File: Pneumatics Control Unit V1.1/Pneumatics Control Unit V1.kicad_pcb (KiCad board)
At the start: 2 copper layers, 53.6 x 65.4 mm, 80 parts, among them J1 TX_PORT, J10 Conn_01x02_Male, J11 Conn_01x02_Male, J12 10118194-0001LF, J2 RX_PORT, J3 MICROMOD-2222, J4 Conn_01x02_Male, J5 Conn_01x02_Male, J6 Conn_01x02_Male, J7 Conn_01x02_Male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

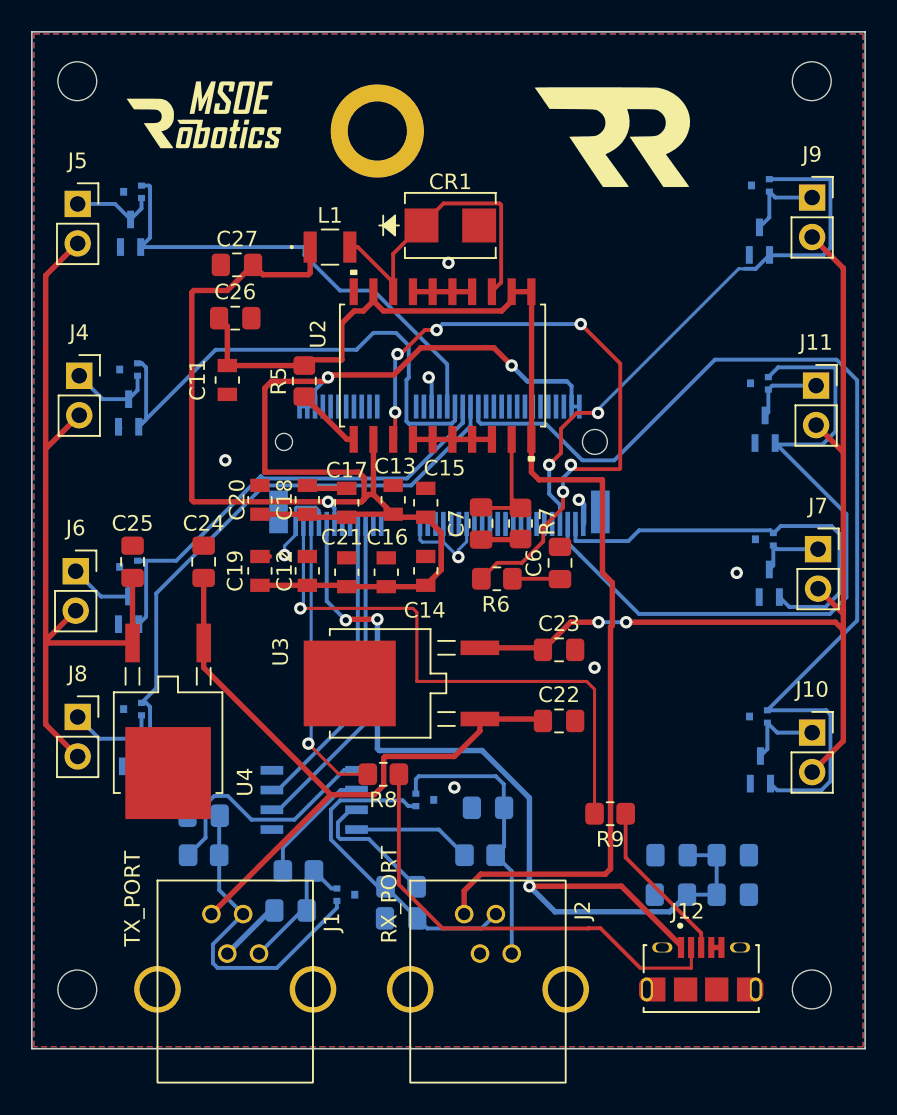
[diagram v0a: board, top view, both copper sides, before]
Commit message: Adding more grounding vias, and making the mouting holes 8-32
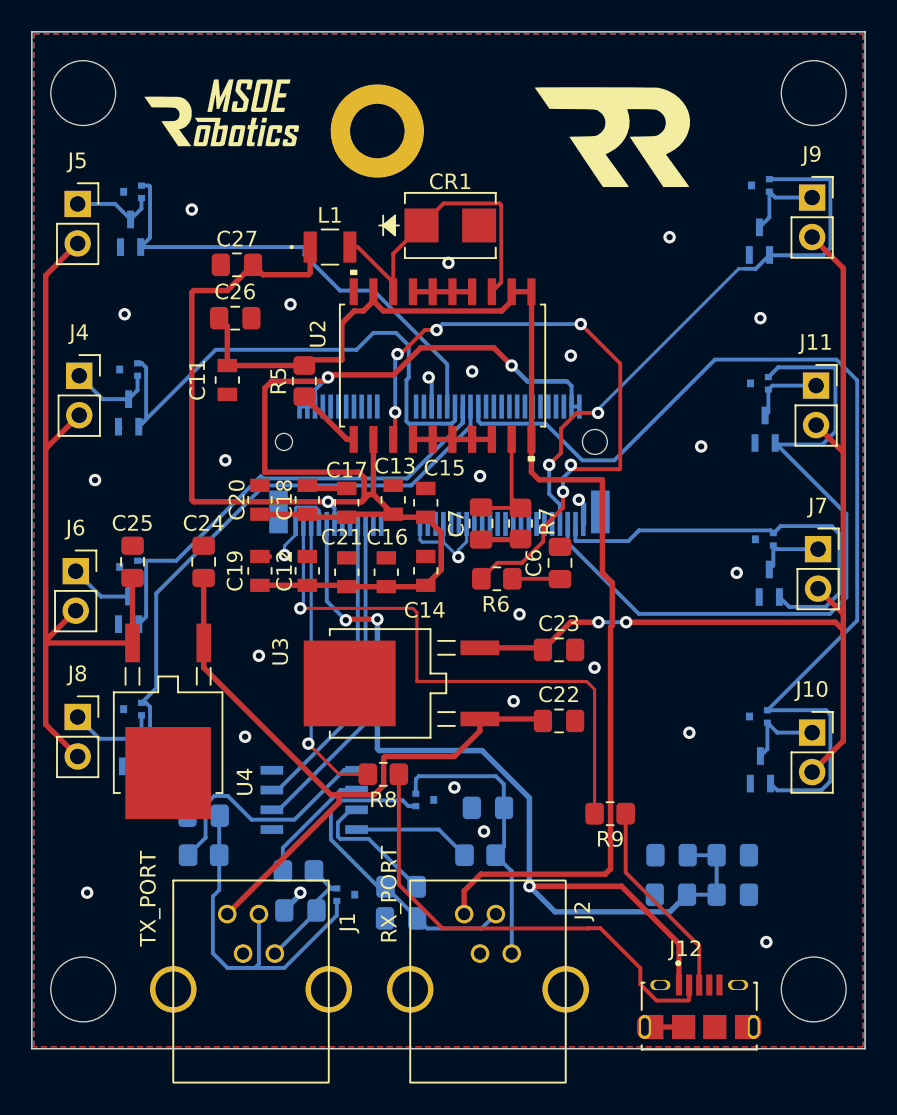
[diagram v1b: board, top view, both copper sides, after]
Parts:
- moved J12 2.42 mm to (146.7, 129.4)
- moved G*** 1.15 mm to (116.0, 70.6)
- moved J1 1.02 mm to (117.9, 128.7)
- moved H2 0.85 mm to (107.1, 69.3)
- moved H1 0.77 mm to (154.1, 69.3)
- moved C3 0.64 mm to (121.0, 121.9)
- moved H4 0.38 mm to (107.1, 127.0)
- moved H3 0.13 mm to (154.1, 127.0)
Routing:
- net USB_V: track 62.9 -> 65.2 mm
- net Net-(J12-Pad3): track 10.6 -> 13.0 mm
- net Net-(C1-Pad1): track 21.1 -> 23.3 mm
- net GND: track 38.1 -> 36.9 mm, vias 9 -> 28
- net Net-(J12-Pad2): track 29.5 -> 30.4 mm
- net Net-(C3-Pad1): track 8.89 -> 8.06 mm

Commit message: Adding Raider Robotics, removing Vex U
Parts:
- removed the G*** at (116.0, 70.6)
- removed the G*** at (143.0, 74.5)

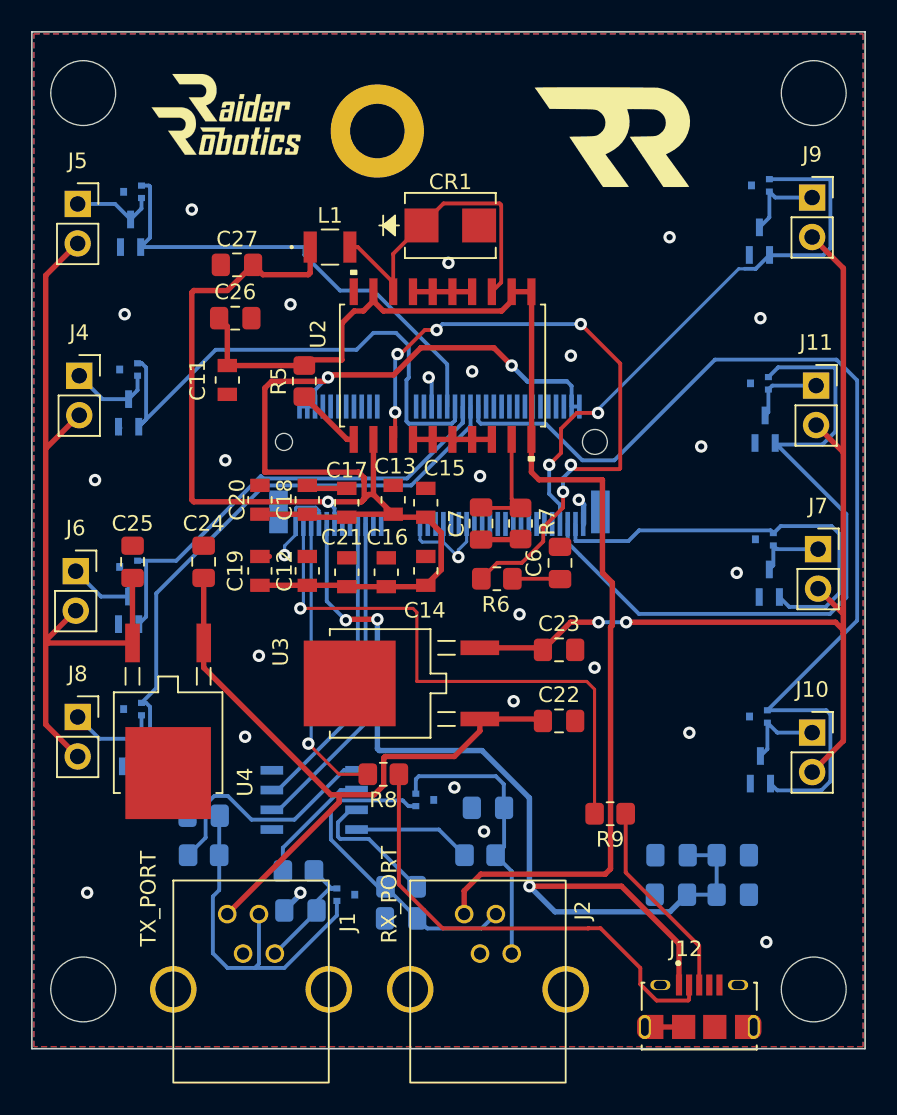
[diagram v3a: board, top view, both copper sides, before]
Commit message: Adding 12V capabilities
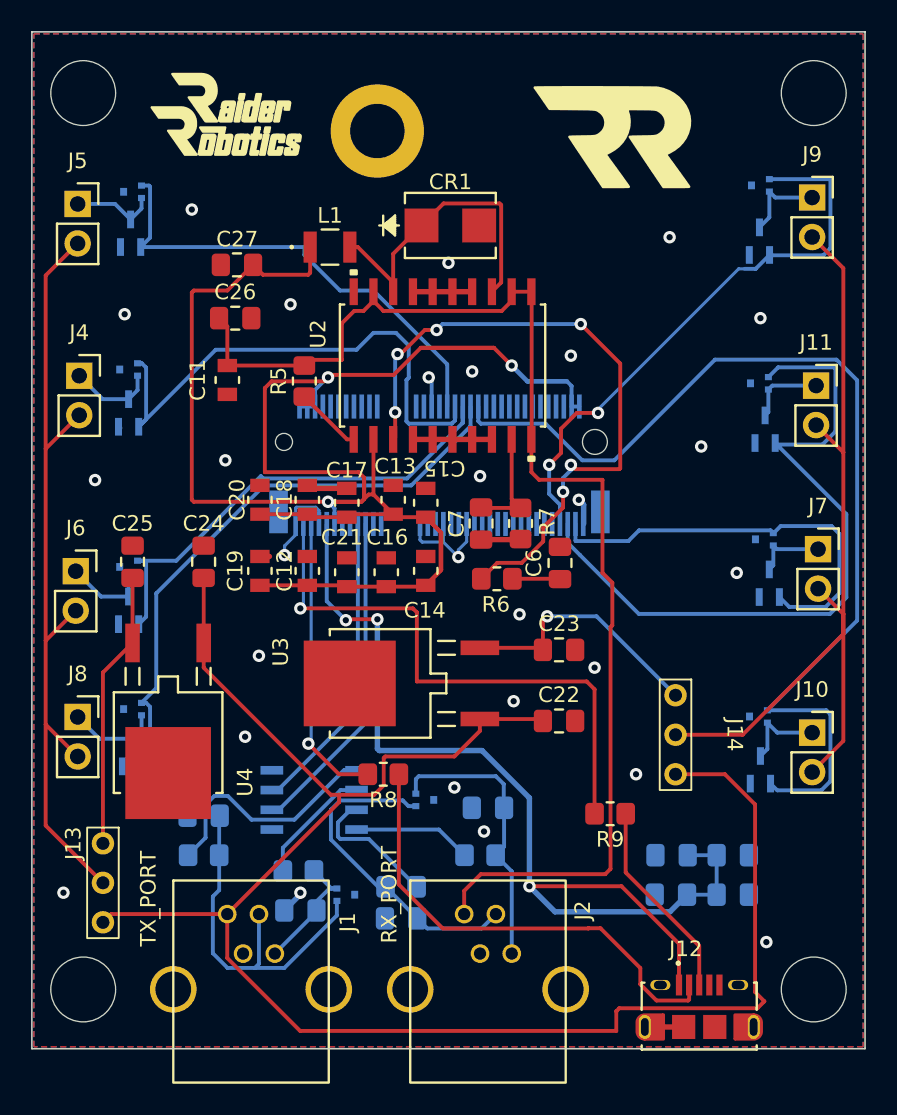
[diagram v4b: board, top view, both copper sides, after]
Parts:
- added J13: Conn_01x03_Male, Header:Conn_1x3, F.Cu at (108.3, 117.6)
- added J14: Conn_01x03_Male, Header:Conn_1x3, F.Cu at (145.2, 108.1)
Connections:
- net 3.3V renamed /220uF
- C10 pad 1: USB_V -> Net-(C10-Pad1)
- C5 pad 1: USB_V -> Net-(C10-Pad1)
- C8 pad 1: USB_V -> Net-(C10-Pad1)
- C9 pad 1: USB_V -> Net-(C10-Pad1)
- J10 pad 2: 5V_R -> /solenoid_power_2
- J11 pad 2: 5V_R -> /solenoid_power_2
- J12 pad 1: USB_V -> Net-(J12-Pad1)
- J3 pad 9: USB_V -> Net-(J3-USB_VIN)
- J4 pad 2: 5V_L -> /solenoid_power
- J5 pad 2: 5V_L -> /solenoid_power
- J6 pad 2: 5V_L -> /solenoid_power
- J7 pad 2: 5V_R -> /solenoid_power_2
- J8 pad 2: 5V_L -> /solenoid_power
- J9 pad 2: 5V_R -> /solenoid_power_2
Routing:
- net /RS485_B_12V: track 45.0 -> 112.9 mm
- net USB_V: track 65.2 -> 0.00 mm, vias 3 -> 0
- net Net-(C10-Pad1): track 0.00 -> 65.2 mm, vias 0 -> 3
- net /solenoid_power_2: track 0.00 -> 55.6 mm
- net /solenoid_power: track 0.00 -> 52.2 mm
- net 5V_R: track 66.5 -> 16.7 mm, vias 2 -> 1
- net 5V_L: track 50.3 -> 17.9 mm

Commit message: Fixing a few ghosts from old projects, and adding inner copper
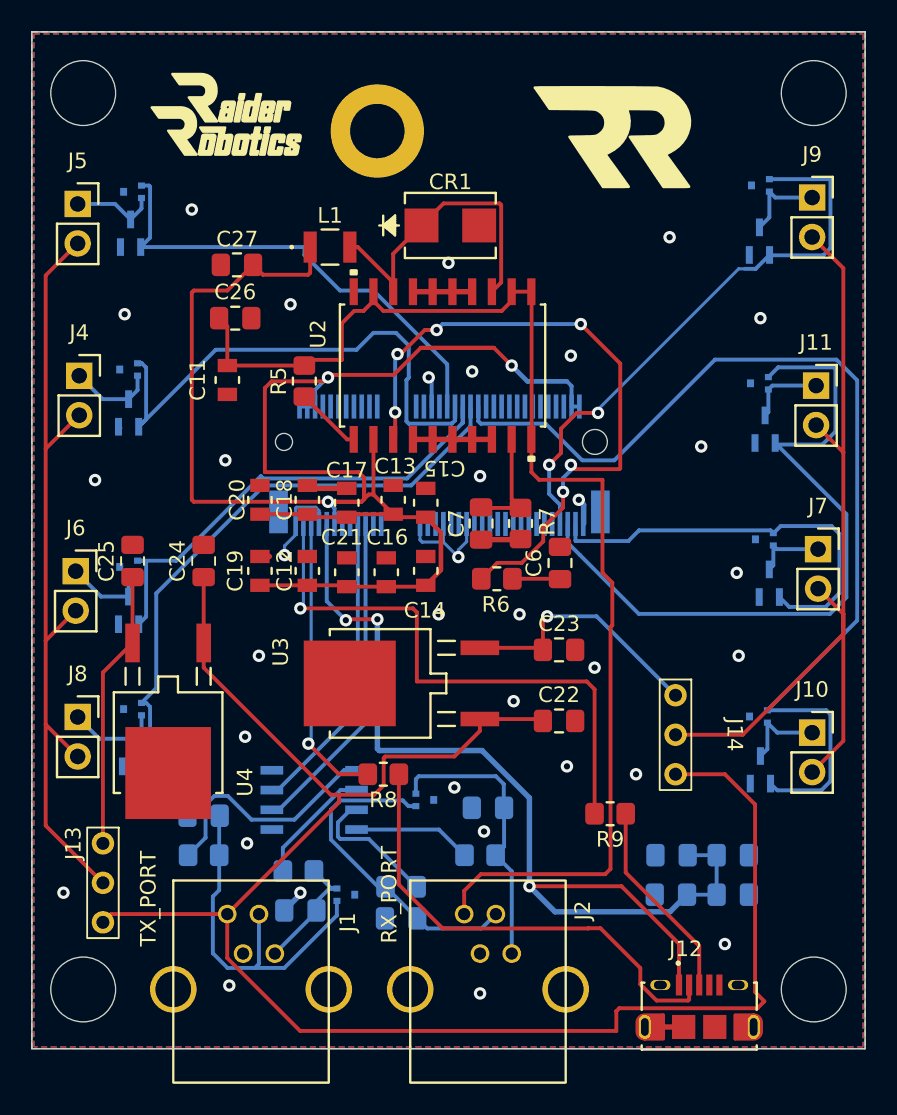
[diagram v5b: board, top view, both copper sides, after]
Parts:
- moved C24 0.05 mm to (114.8, 99.4)
- moved C25 0.05 mm to (110.2, 99.4)
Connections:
- net 5V_L renamed Net-(U4-OUTPUT)
- C23 pad 1: 5V_R -> Net-(U3-OUTPUT)
- J14 pad 1: 5V_R -> Net-(J14-Pin_1)
- U3 pad 3: 5V_R -> Net-(U3-OUTPUT)
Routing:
- net Net-(U3-OUTPUT): track 0.00 -> 16.7 mm, vias 0 -> 1
- net 5V_R: track 16.7 -> 0.00 mm, vias 1 -> 0
- net GND: vias 28 -> 34
- added copper zone on In1.Cu, net (none)
- added copper zone on In2.Cu, net (none)
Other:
- copper layers 2 -> 4
